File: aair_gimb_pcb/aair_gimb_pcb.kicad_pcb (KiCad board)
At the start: 2 copper layers, 6 parts, among them SW1 SW_Push, SW2 SW_Push, U1 STM32F405RGTx, X1 8MHz

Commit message: mac update
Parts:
- C1, C2: footprint Capacitor_SMD:C_0201_0603Metric_Pad0.64x0.40mm_HandSolder -> CRF1:SMD-0603_c
- SW1, SW2: footprint Button_Switch_THT:SW_PUSH_6mm_H5mm -> Button_Switch_SMD:SW_Push_1P1T_NO_CK_KMR2
- X1: footprint Crystal:Crystal_SMD_Abracon_ABM10-4Pin_2.5x2.0mm -> CRF1:Crystal_5x3mm
- moved SW2 27.9 mm to (87.0, 68.0), turned to 90 degrees
- moved SW1 27.2 mm to (93.0, 68.0), turned to 90 degrees
- moved X1 5.02 mm to (79.0, 81.0), turned to -90 degrees
- moved C2 2.83 mm to (81.7, 71.5)
- moved C1 2.00 mm to (81.7, 74.0)

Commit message: macros
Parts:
- removed SW1, SW2: SW_Push, Button_Switch_SMD:SW_Push_1P1T_NO_CK_KMR2
- removed X1: 8MHz, CRF1:Crystal_5x3mm
- added B1: SW_Push, Button_Switch_SMD:SW_Push_1P1T_NO_CK_KMR2, F.Cu at (147.8, 89.9)
- added C10: 15p, CRF1:SMD-0603_c, F.Cu at (147.8, 85.1)
- added C11: 2.2u, CRF1:SMD-0603_r, F.Cu at (173.2, 64.9)
- added C12: 2.2u, CRF1:SMD-0603_c, F.Cu at (173.2, 77.5)
- added C13: 2.2u, CRF1:SMD-0603_r, F.Cu at (173.2, 67.5)
- added C14: 2.2u, CRF1:SMD-0603_r, F.Cu at (173.2, 70.0)
- added C15: 2.2u, CRF1:SMD-0603_r, F.Cu at (173.2, 75.0)
- added C16: 2.2u, CRF1:SMD-0603_r, F.Cu at (173.2, 72.5)
- added C3: 2.2u, CRF1:SMD-0603_r, F.Cu at (167.7, 70.0)
- added C4: 2.2u, CRF1:SMD-0603_r, F.Cu at (167.7, 72.5)
- added C5: 2.2u, CRF1:SMD-0603_c, F.Cu at (167.7, 75.0)
- added C6: 2.2u, CRF1:SMD-0603_r, F.Cu at (167.7, 77.5)
- added C9: 15p, CRF1:SMD-0603_c, F.Cu at (147.8, 82.7)
- added D2: LED, LED_SMD:LED_0603_1608Metric, F.Cu at (153.2, 93.5)
- added J3: USB_B_Mini, Connector_USB:USB_Mini-B_Lumberg_2486_01_Horizontal, F.Cu at (138.0, 92.3)
- added J4: SWD, Connector_PinHeader_1.27mm:PinHeader_2x05_P1.27mm_Vertical_SMD, F.Cu at (150.8, 77.3)
- added NR1: SW_Push, Button_Switch_SMD:SW_Push_1P1T_NO_CK_KMR2, F.Cu at (147.8, 94.5)
- added R2: R_Small, Resistor_SMD:R_0603_1608Metric, F.Cu at (153.2, 96.0)
- added U2: STM32F405RGTx, Package_QFP:LQFP-64_10x10mm_P0.5mm, F.Cu at (138.8, 80.3)
- added U4: USBLC6-2SC6, Package_TO_SOT_SMD:SOT-23-6, F.Cu at (153.7, 89.9)
- added X2: 8MHz, CRF1:Crystal_5x3mm, F.Cu at (152.8, 83.8)
- C1: value 15p -> 22n; footprint CRF1:SMD-0603_c -> CRF1:SMD-0603_r
- C2: value 15p -> 2.2u; footprint CRF1:SMD-0603_c -> CRF1:SMD-0603_r
- U1: value STM32F405RGTx -> DRV8302; footprint Package_QFP:LQFP-64_10x10mm_P0.5mm -> CRF1:TSSOP-56-PP
- moved C1 86.4 mm to (167.7, 64.9)
- moved C2 86.1 mm to (167.7, 67.5)
- moved U1 78.0 mm to (167.7, 85.0)
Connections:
- C1 pad 1: Net-(U1-PH0) -> Net-(U1-CP1)
- C1 pad 2: GND -> Net-(U1-CP2)
- C2 pad 1: Net-(U1-PH1) -> Net-(U1-AVDD)
- U1 pad 10: unconnected-(U1-PC2-Pad10) -> /drv8302/GAIN
- U1 pad 11: unconnected-(U1-PC3-Pad11) -> Net-(U1-DVDD)
- U1 pad 12: unconnected-(U1-VSSA-Pad12) -> /drv8302/DC_CAL
- U1 pad 13: unconnected-(U1-VDDA-Pad13) -> Net-(U1-GVDD)
- U1 pad 14: unconnected-(U1-PA0-Pad14) -> Net-(U1-CP1)
- U1 pad 15: unconnected-(U1-PA1-Pad15) -> Net-(U1-CP2)
- U1 pad 16: unconnected-(U1-PA2-Pad16) -> /drv8302/EN_GATE
- U1 pad 17: unconnected-(U1-PA3-Pad17) -> /drv8302/H1
- U1 pad 18: Net-(U1-VSS-Pad18) -> /Stm32f405/L1
- U1 pad 19: unconnected-(U1-VDD-Pad19) -> /drv8302/H2
- U1 pad 20: unconnected-(U1-PA4-Pad20) -> /Stm32f405/L2
- U1 pad 21: unconnected-(U1-PA5-Pad21) -> /drv8302/H3
- U1 pad 22: unconnected-(U1-PA6-Pad22) -> /Stm32f405/L3
- U1 pad 23: unconnected-(U1-PA7-Pad23) -> Net-(U1-DVDD)
- U1 pad 24: unconnected-(U1-PC4-Pad24) -> VCC
- U1 pad 25: unconnected-(U1-PC5-Pad25) -> /drv8302/Current_ADC_1
- U1 pad 26: unconnected-(U1-PB0-Pad26) -> /drv8302/Current_ADC_2
- U1 pad 27: unconnected-(U1-PB1-Pad27) -> Net-(U1-AVDD)
- U1 pad 28: unconnected-(U1-PB2-Pad28) -> GND
- U1 pad 5: Net-(U1-PH0) -> unconnected-(U1-OCTW-Pad5)
- U1 pad 57: unconnected-(U1-PB5-Pad57) -> GND
- U1 pad 6: Net-(U1-PH1) -> /drv8302/FAULT
- U1 pad 7: Net-(U1-NRST) -> unconnected-(U1-DTC-Pad7)
- U1 pad 8: unconnected-(U1-PC0-Pad8) -> /drv8302/M_PWM

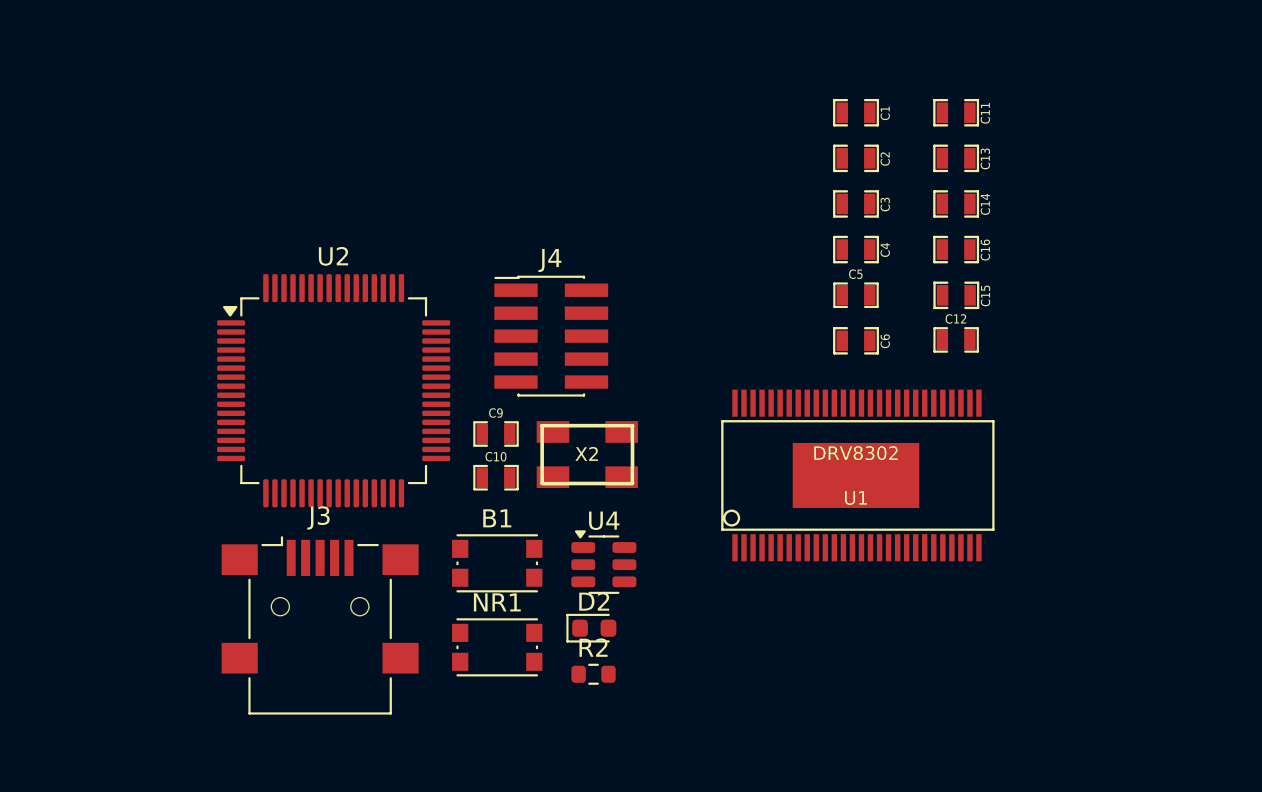
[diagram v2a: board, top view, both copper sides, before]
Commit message: add mosfet
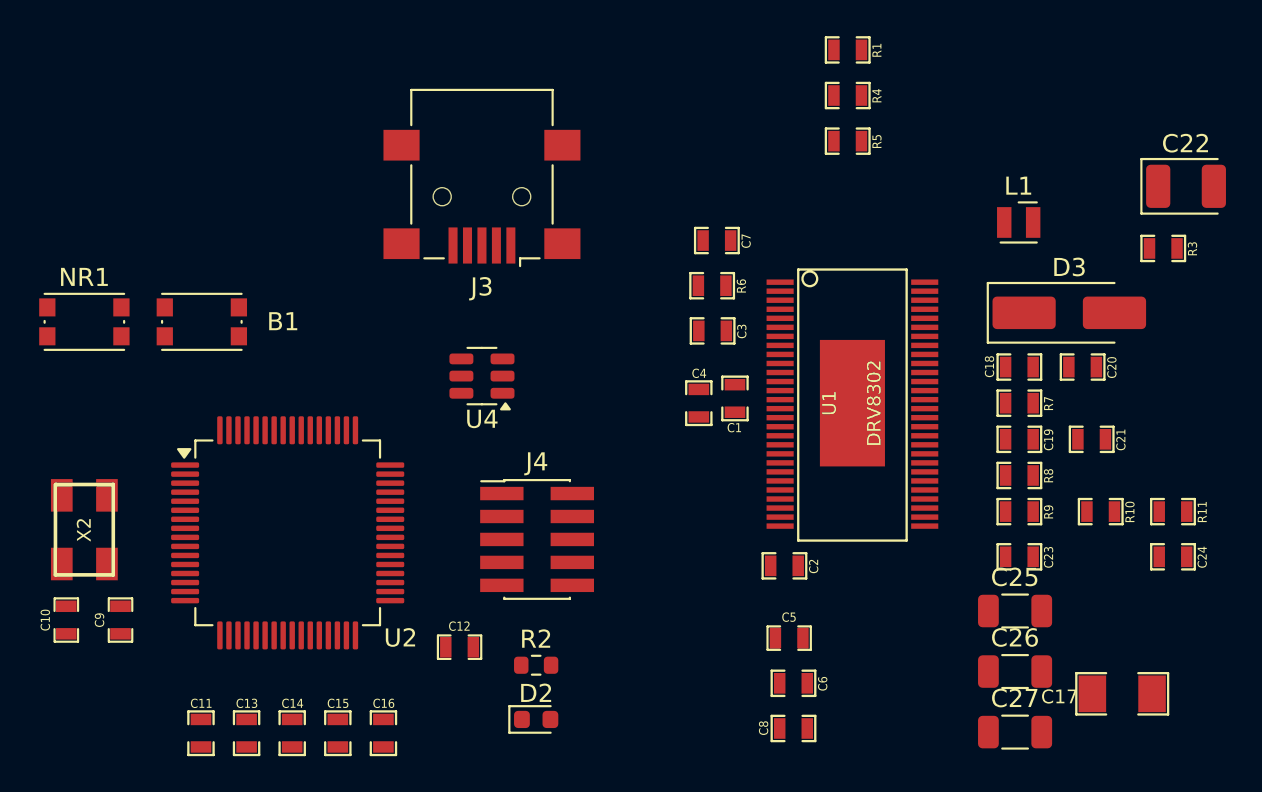
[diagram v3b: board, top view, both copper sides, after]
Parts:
- added C17: 10u, 50V, CRF1:SMD-1206, F.Cu at (182.4, 97.1)
- added C18: 100n, CRF1:SMD-0603_r, F.Cu at (176.7, 79.0)
- added C19: 220n, CRF1:SMD-0603_r, F.Cu at (176.7, 83.0)
- added C20: 220n, CRF1:SMD-0603_r, F.Cu at (180.2, 79.0)
- added C21: 220n, CRF1:SMD-0603_r, F.Cu at (180.7, 83.0)
- added C22: C_Polarized_Small_US, Capacitor_Tantalum_SMD:CP_EIA-3528-21_Kemet-B, F.Cu at (186.0, 69.0)
- added C23: 2.2n, CRF1:SMD-0603_r, F.Cu at (176.7, 89.5)
- added C24: 2.2n, CRF1:SMD-0603_r, F.Cu at (185.2, 89.5)
- added C25: 10u,50v, Capacitor_SMD:C_1206_3216Metric, F.Cu at (176.5, 92.5)
- added C26: 10u,50v, Capacitor_SMD:C_1206_3216Metric, F.Cu at (176.5, 95.8)
- added C27: 10u,50v, Capacitor_SMD:C_1206_3216Metric, F.Cu at (176.5, 99.2)
- added C7: 120p, CRF1:SMD-0603_r, F.Cu at (160.0, 72.0)
- added C8: 6.8n, CRF1:SMD-0603_r, F.Cu at (164.2, 99.0)
- added D3: D_Schottky, Diode_SMD:D_SMA_Handsoldering, F.Cu at (179.5, 76.0)
- added L1: L, Inductor_SMD_Wurth:L_Wurth_WE-LQSH-2010, F.Cu at (176.7, 71.0)
- added R1: 10k, CRF1:SMD-0603_r, F.Cu at (167.2, 61.5)
- added R10: 100, CRF1:SMD-0603_r, F.Cu at (181.2, 87.0)
- added R11: 100, CRF1:SMD-0603_r, F.Cu at (185.2, 87.0)
- added R3: 3.3k, CRF1:SMD-0603_r, F.Cu at (184.7, 72.4)
- added R4: 18k, CRF1:SMD-0603_r, F.Cu at (167.2, 64.0)
- added R5: 15k, CRF1:SMD-0603_r, F.Cu at (167.2, 66.5)
- added R6: 220k, CRF1:SMD-0603_r, F.Cu at (159.7, 74.5)
- added R7: 1M, CRF1:SMD-0603_r, F.Cu at (176.7, 81.0)
- added R8: 100, CRF1:SMD-0603_r, F.Cu at (176.7, 85.0)
- added R9: 100, CRF1:SMD-0603_r, F.Cu at (176.7, 87.0)
- moved C11 54.1 mm to (131.5, 99.3), turned to 90 degrees
- moved C13 50.5 mm to (134.0, 99.3), turned to 90 degrees
- moved C14 47.0 mm to (136.5, 99.3), turned to 90 degrees
- moved C15 41.9 mm to (139.0, 99.3), turned to 90 degrees
- moved C16 41.5 mm to (141.5, 99.3), turned to 90 degrees
- moved C12 32.3 mm to (145.8, 94.5)
- moved NR1 29.1 mm to (125.0, 76.5)
- moved X2 28.1 mm to (125.0, 88.0), turned to 90 degrees
- moved C10 25.0 mm to (124.0, 93.0), turned to 90 degrees
- moved J3 24.4 mm to (147.0, 69.6), turned to 180 degrees
- moved C9 23.2 mm to (127.0, 93.0), turned to 90 degrees
- moved C2 22.9 mm to (163.7, 90.0)
- moved B1 21.1 mm to (131.5, 76.5)
- moved C5 19.3 mm to (164.0, 94.0)
- moved C6 19.3 mm to (164.2, 96.5)
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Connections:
- B1 pad 1: GND -> V_SUPPLY
- C10 pad 2: GND -> V_SUPPLY
- C11 pad 1: GND -> V_SUPPLY
- C12 pad 1: GND -> V_SUPPLY
- C13 pad 1: GND -> V_SUPPLY
- C14 pad 1: GND -> V_SUPPLY
- C15 pad 1: GND -> V_SUPPLY
- C16 pad 1: GND -> V_SUPPLY
- C2 pad 2: GND -> V_SUPPLY
- C3 pad 2: GND -> V_SUPPLY
- C4 pad 2: GND -> V_SUPPLY
- C5 pad 2: GND -> V_SUPPLY
- C6 pad 2: GND -> V_SUPPLY
- C9 pad 2: GND -> V_SUPPLY
- J3 pad 5: GND -> V_SUPPLY
- J4 pad 3: GND -> V_SUPPLY
- J4 pad 5: GND -> V_SUPPLY
- J4 pad 9: GND -> V_SUPPLY
- NR1 pad 1: GND -> V_SUPPLY
- R2 pad 2: GND -> V_SUPPLY
- U1 pad 1: unconnected-(U1-RT_CLK-Pad1) -> Net-(U1-RT_CLK)
- U1 pad 2: unconnected-(U1-COMP-Pad2) -> Net-(U1-COMP)
- U1 pad 28: GND -> V_SUPPLY
- U1 pad 29: unconnected-(U1-PVDD1-Pad29) -> V_SUPPLY
- U1 pad 3: unconnected-(U1-VSENSE-Pad3) -> Net-(U1-VSENSE)
- U1 pad 30: unconnected-(U1-SP2-Pad30) -> Net-(U1-SP2)
- U1 pad 31: unconnected-(U1-SN2-Pad31) -> Net-(U1-SN2)
- U1 pad 32: unconnected-(U1-SP1-Pad32) -> Net-(U1-SP1)
- U1 pad 33: unconnected-(U1-SN1-Pad33) -> Net-(U1-SN1)
- U1 pad 34: unconnected-(U1-SL_C-Pad34) -> /drv8302/H3_LOW
- U1 pad 35: unconnected-(U1-GL_C-Pad35) -> /drv8302/M_L3
- U1 pad 36: unconnected-(U1-SH_C-Pad36) -> /drv8302/H3_VS
- U1 pad 37: unconnected-(U1-GH_C-Pad37) -> /drv8302/M_H3
- U1 pad 38: unconnected-(U1-BST_C-Pad38) -> Net-(U1-BST_C)
- U1 pad 39: unconnected-(U1-SL_B-Pad39) -> /drv8302/H2_LOW
- U1 pad 40: unconnected-(U1-GL_B-Pad40) -> /drv8302/M_L2
- U1 pad 41: unconnected-(U1-SH_B-Pad41) -> /drv8302/H2_VS
- U1 pad 42: unconnected-(U1-GH_B-Pad42) -> /drv8302/M_H2
- U1 pad 43: unconnected-(U1-BST_B-Pad43) -> Net-(U1-BST_B)
- U1 pad 44: unconnected-(U1-SL_A-Pad44) -> /drv8302/H1_LOW
- U1 pad 45: unconnected-(U1-GL_A-Pad45) -> /drv8302/M_L1
- U1 pad 46: unconnected-(U1-SH_A-Pad46) -> /drv8302/H1_VS
- U1 pad 47: unconnected-(U1-GH_A-Pad47) -> /drv8302/M_H1
- U1 pad 48: unconnected-(U1-BST_A-Pad48) -> Net-(U1-BST_A)
- U1 pad 49: unconnected-(U1-BIAS-Pad49) -> Net-(U1-BIAS)
- U1 pad 50: unconnected-(U1-PH-Pad50) -> Net-(D3-K)
- U1 pad 51: unconnected-(U1-PH-Pad51) -> Net-(D3-K)
- U1 pad 52: unconnected-(U1-BST_BK-Pad52) -> Net-(U1-BST_BK)
- U1 pad 53: unconnected-(U1-PVDD2-Pad53) -> Net-(C17-Pad2)
- U1 pad 54: unconnected-(U1-PVDD2-Pad54) -> Net-(C17-Pad2)
- U1 pad 57: GND -> V_SUPPLY
- U1 pad 7: unconnected-(U1-DTC-Pad7) -> Net-(U1-DTC)
- U1 pad 9: unconnected-(U1-M_OC-Pad9) -> VCC
- U2 pad 12: GND -> V_SUPPLY
- U2 pad 18: GND -> V_SUPPLY
- U2 pad 63: GND -> V_SUPPLY
- U4 pad 2: GND -> V_SUPPLY
- X2 pad 3: GND -> V_SUPPLY

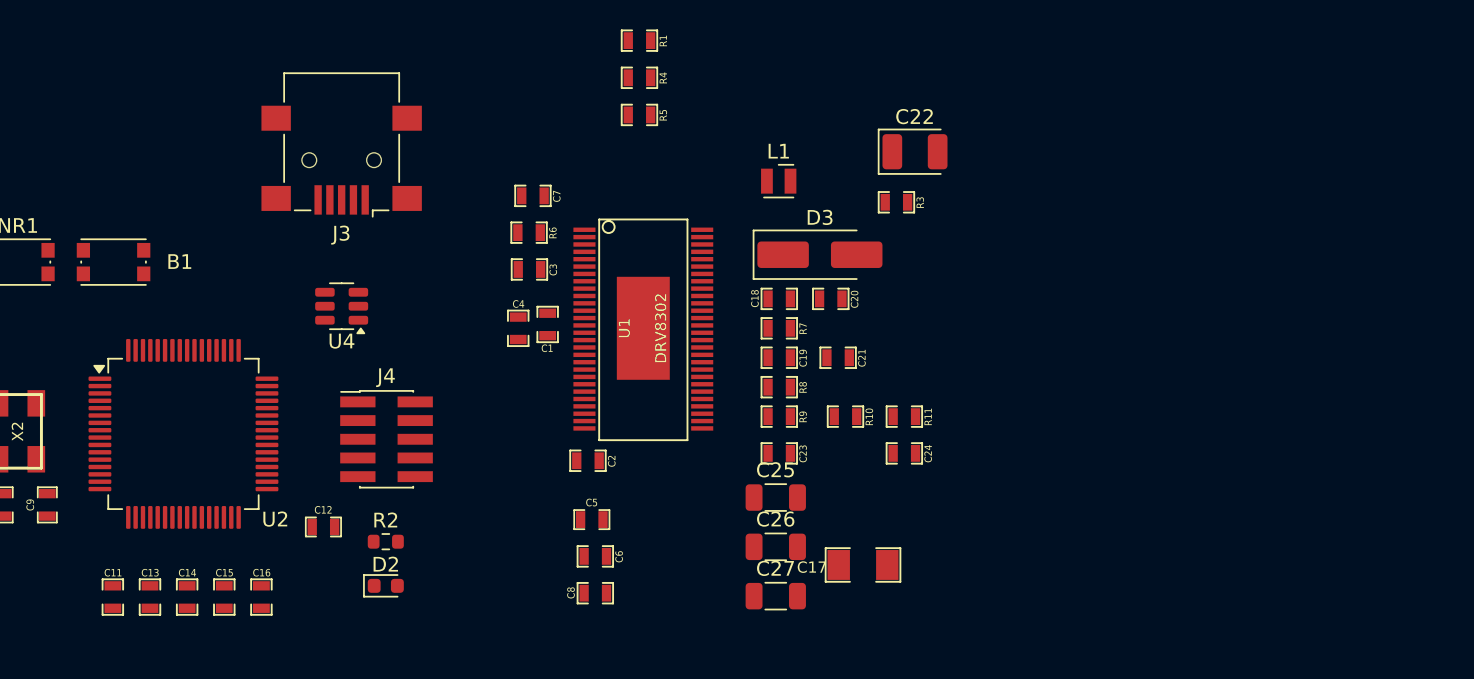
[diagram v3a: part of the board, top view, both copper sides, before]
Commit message: добавить пины стм, диод, питание 3.3, разъемы
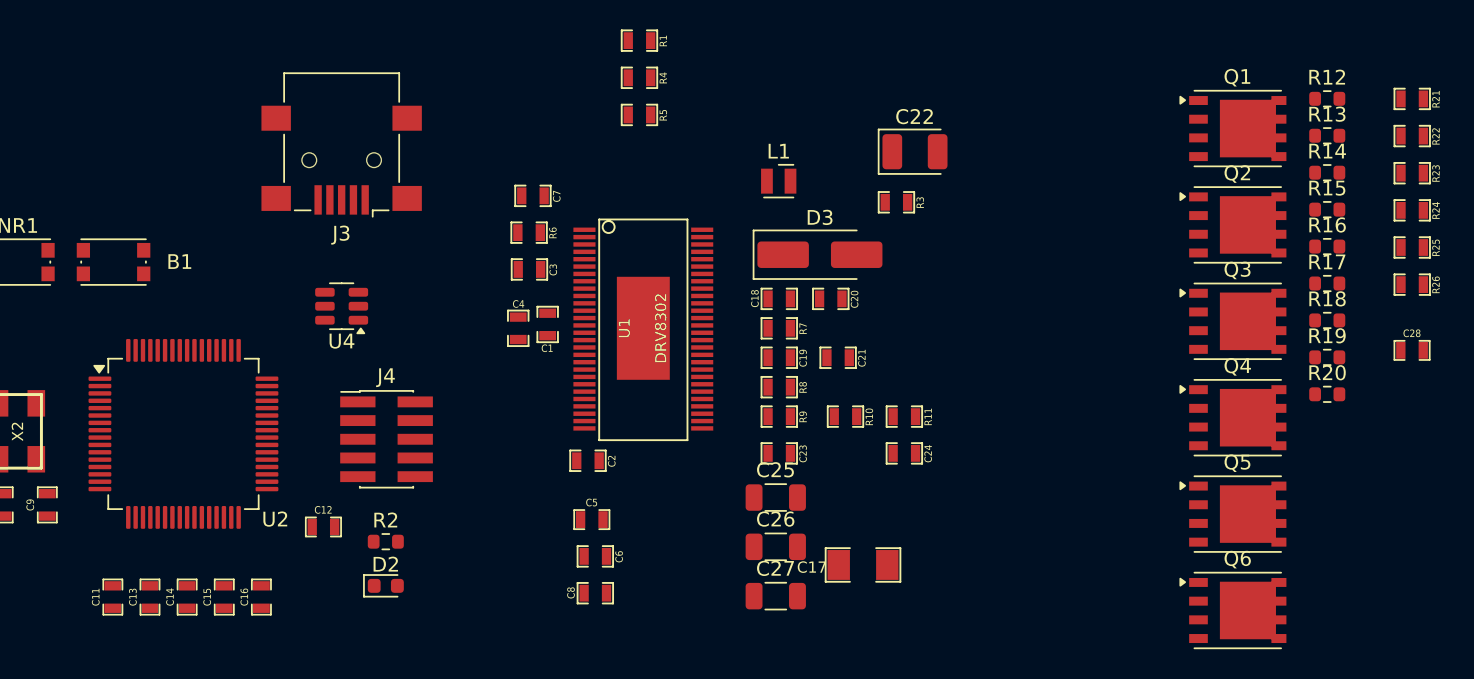
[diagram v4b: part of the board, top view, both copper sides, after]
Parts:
- added C28: 2.2u, CRF1:SMD-0603_c, F.Cu at (219.7, 82.5)
- added Q1: sir182dp, Package_SO:PowerPAK_SO-8_Single, F.Cu at (207.9, 67.4)
- added Q2: sir182dp, Package_SO:PowerPAK_SO-8_Single, F.Cu at (207.9, 74.0)
- added Q3: sir182dp, Package_SO:PowerPAK_SO-8_Single, F.Cu at (207.9, 80.5)
- added Q4: sir182dp, Package_SO:PowerPAK_SO-8_Single, F.Cu at (207.9, 87.1)
- added Q5: sir182dp, Package_SO:PowerPAK_SO-8_Single, F.Cu at (207.9, 93.6)
- added Q6: sir182dp, Package_SO:PowerPAK_SO-8_Single, F.Cu at (207.9, 100.2)
- added R12: 4.7, Resistor_SMD:R_0603_1608Metric, F.Cu at (214.0, 65.4)
- added R13: 4.7, Resistor_SMD:R_0603_1608Metric, F.Cu at (214.0, 67.9)
- added R14: 4.7, Resistor_SMD:R_0603_1608Metric, F.Cu at (214.0, 70.4)
- added R15: 4.7, Resistor_SMD:R_0603_1608Metric, F.Cu at (214.0, 72.9)
- added R16: 4.7, Resistor_SMD:R_0603_1608Metric, F.Cu at (214.0, 75.4)
- added R17: 4.7, Resistor_SMD:R_0603_1608Metric, F.Cu at (214.0, 78.0)
- added R18: 39k, Resistor_SMD:R_0603_1608Metric, F.Cu at (214.0, 80.5)
- added R19: 39k, Resistor_SMD:R_0603_1608Metric, F.Cu at (214.0, 83.0)
- added R20: 39k, Resistor_SMD:R_0603_1608Metric, F.Cu at (214.0, 85.5)
- added R21: 39k, CRF1:SMD-0603_r, F.Cu at (219.7, 65.4)
- added R22: 39k, CRF1:SMD-0603_r, F.Cu at (219.7, 67.9)
- added R23: 39k, CRF1:SMD-0603_r, F.Cu at (219.7, 70.5)
- added R24: 2.2k, CRF1:SMD-0603_r, F.Cu at (219.7, 73.0)
- added R25: 2.2k, CRF1:SMD-0603_r, F.Cu at (219.7, 75.5)
- added R26: 2.2k, CRF1:SMD-0603_r, F.Cu at (219.7, 78.0)
- C11, C13, C14, C15, C16: footprint CRF1:SMD-0603_r -> CRF1:SMD-0603_c
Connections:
- C13 pad 2: VCC -> +3.3V
- C14 pad 2: VCC -> +3.3V
- C15 pad 2: VCC -> +3.3V
- C16 pad 2: VCC -> +3.3V
- U1 pad 17: /drv8302/H1 -> /Stm32f405/H1
- U1 pad 19: /drv8302/H2 -> /Stm32f405/H2
- U1 pad 21: /drv8302/H3 -> /Stm32f405/H3
- U2 pad 1: VCC -> +3.3V
- U2 pad 13: VCC -> +3.3V
- U2 pad 19: VCC -> +3.3V
- U2 pad 32: VCC -> +3.3V
- U2 pad 48: VCC -> +3.3V
- U2 pad 64: VCC -> +3.3V
